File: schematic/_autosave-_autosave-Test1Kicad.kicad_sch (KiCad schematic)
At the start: 40 parts, among them IC1 BMI055, J1 Power Module 1, J2 Power Module 2, J3 USB, J4 Telemetry 1, J5 Telemetry 2, J6 UART & I2C B, J7 CAN 1, J8 CAN 2, U1 STM32F765IIKx, U10 TJA1051TK-3, U2 NEO-M8N, U3 IST8310, U4 ICM-20602, U5 ICM-20689, U6 MS5611-01BA, U7 LT3080xDD, U8 STM32F103V8Tx, U9 TJA1051TK-3, Y1 ABM2-8.000MHZ-D4Y-T

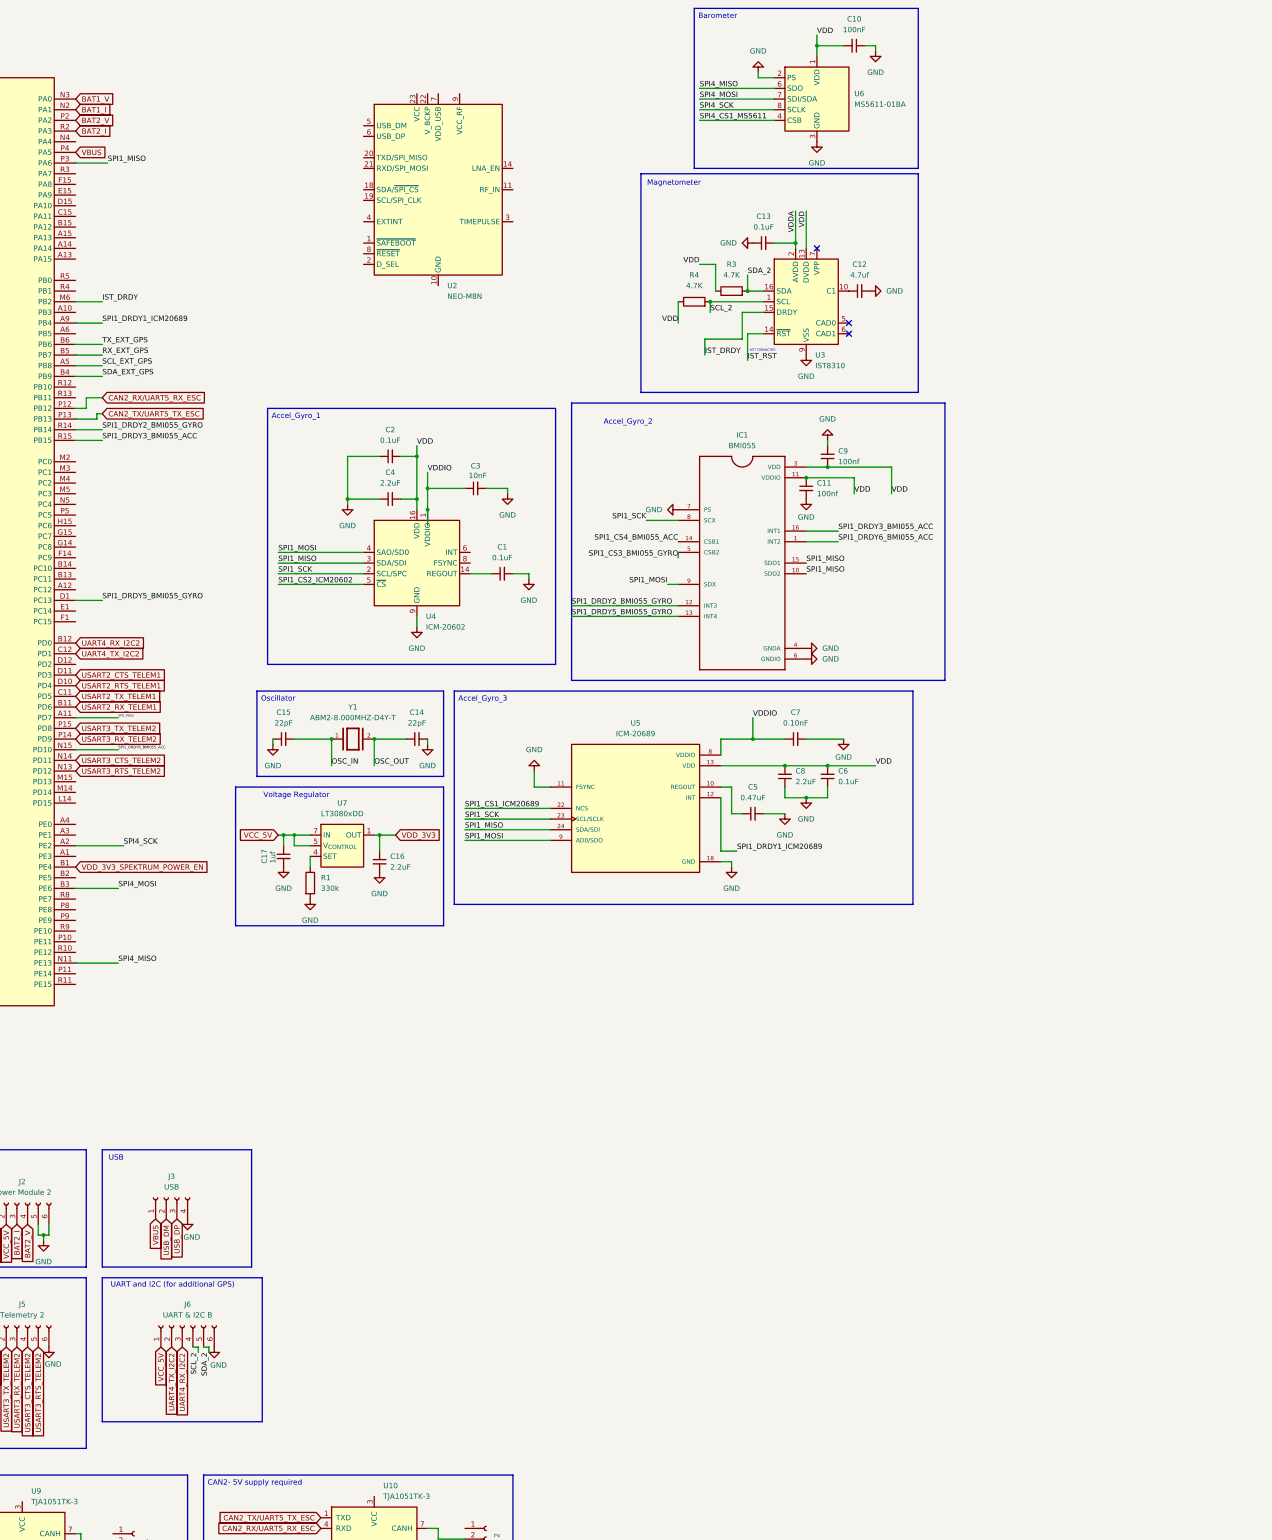
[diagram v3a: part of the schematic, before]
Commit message: GPS module port, led, piezo buzzer (not fully connected)
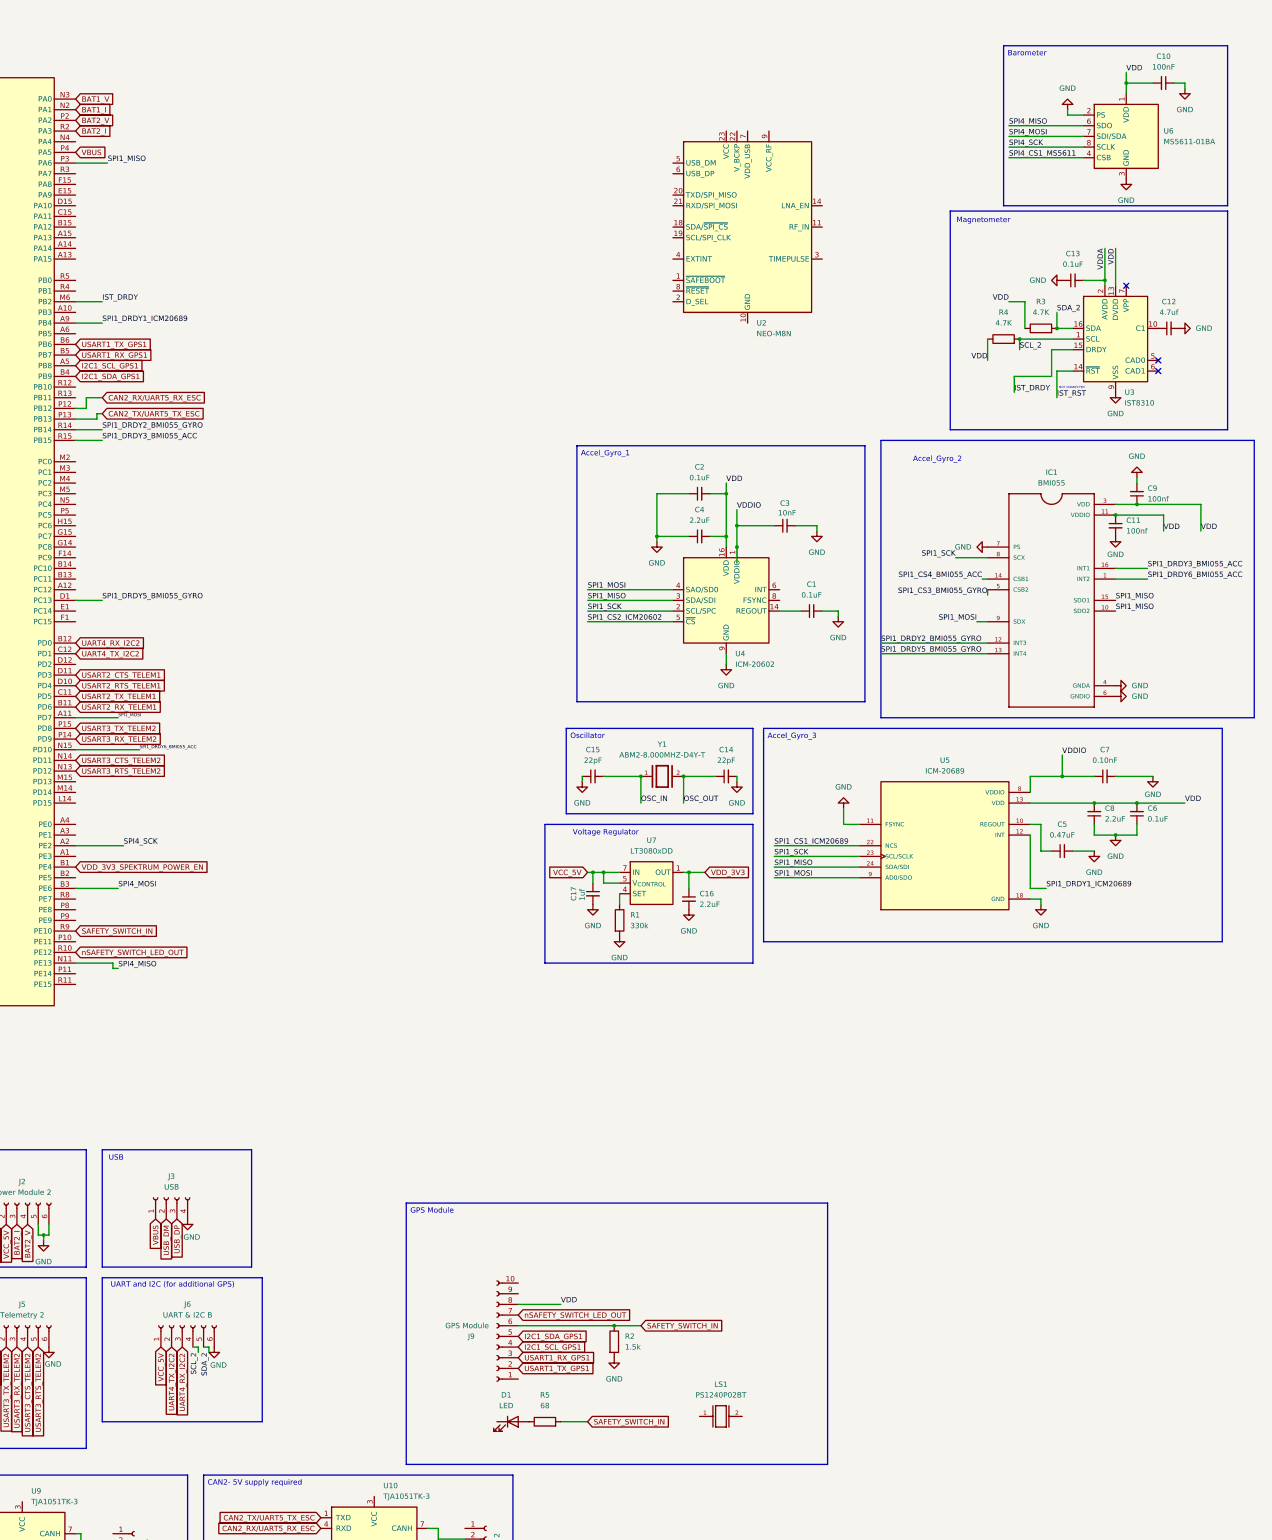
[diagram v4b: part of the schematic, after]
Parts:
- added D1: LED, symbol Device:LED
- added J9: GPS Module, symbol Connector:Conn_01x10_Socket
- added LS1: PS1240P02BT, PS1240P02BT:XDCR_PS1240P02BT, symbol PS1240P02BT:PS1240P02BT
- added R2: 1.5k, symbol Device:R
- added R5: 68, symbol Device:R
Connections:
- net GND: now also R2.2
- net VDD: now also J9.8 (Pin_8)
- net nSAFETY_SWITCH_LED_OUT: now reaches U1.R10 (PE12)
- net nSAFETY_SWITCH_LED_OUT: now also J9.7 (Pin_7)
- net SAFETY_SWITCH_IN: now reaches U1.R9 (PE10)
- net SAFETY_SWITCH_IN: now also J9.6 (Pin_6), R2.1, R5.2
- net RX_EXT_GPS renamed USART1_RX_GPS1
- net USART1_RX_GPS1: now also J9.3 (Pin_3)
- net SCL_EXT_GPS renamed I2C1_SCL_GPS1
- net I2C1_SCL_GPS1: now also J9.4 (Pin_4)
- net SDA_EXT_GPS renamed I2C1_SDA_GPS1
- net I2C1_SDA_GPS1: now also J9.5 (Pin_5)
- net TX_EXT_GPS renamed USART1_TX_GPS1
- net USART1_TX_GPS1: now also J9.2 (Pin_2)
- new net: D1.2 (A), R5.1
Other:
- moved on the sheet: C1, C10, C11, C12, C13, C14, C15, C16, C17, C2, C3, C4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
